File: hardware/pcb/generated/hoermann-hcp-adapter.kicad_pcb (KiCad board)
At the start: 2 copper layers, 65 x 44.5 mm, 6 parts, among them J1 HCP2 6P6C, U1 ESP32-C3 Super Mini, U2 Isolated RS485

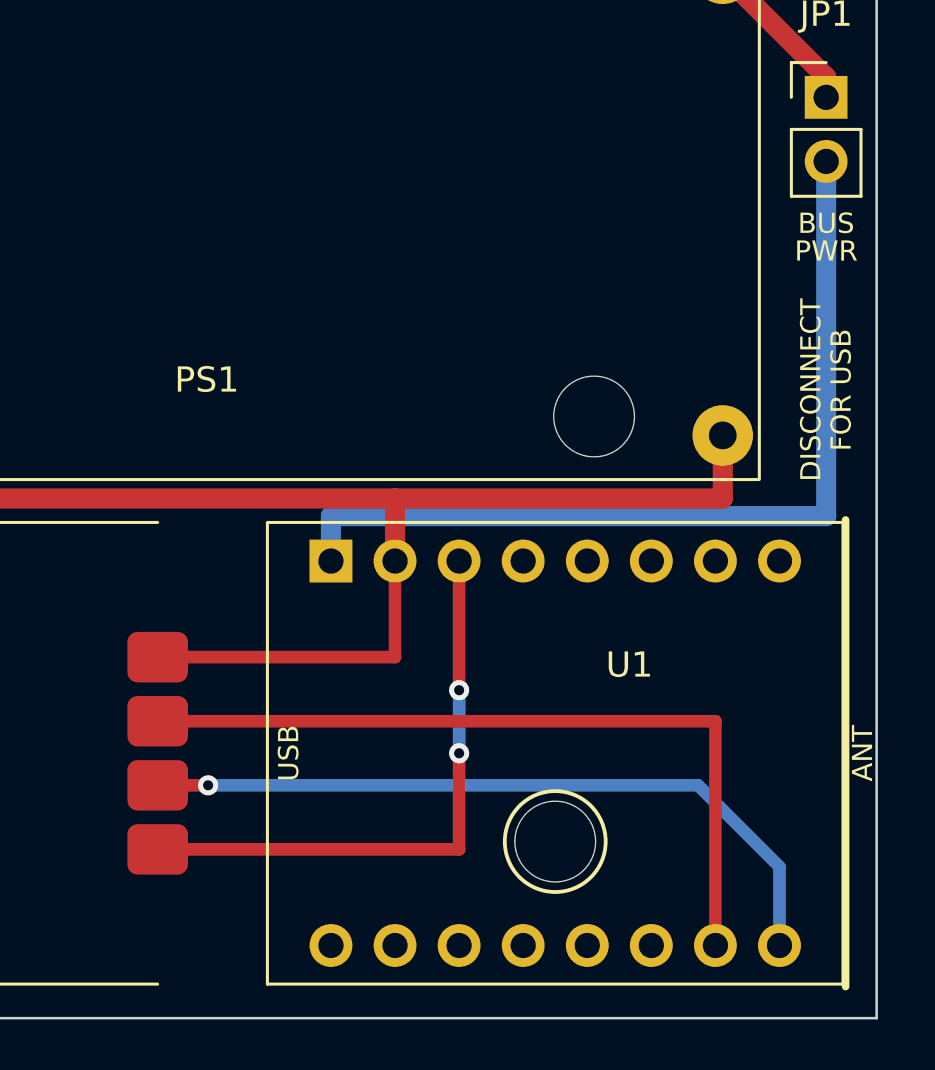
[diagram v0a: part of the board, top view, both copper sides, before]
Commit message: Put the ESP32 USB port at the board edge
U1 is rotated so its USB end sits flush with the right edge and stays
usable when mounted. The antenna now points towards the RS485 module.

Co-Authored-By: Claude Fable 5.1 <noreply@anthropic.com>
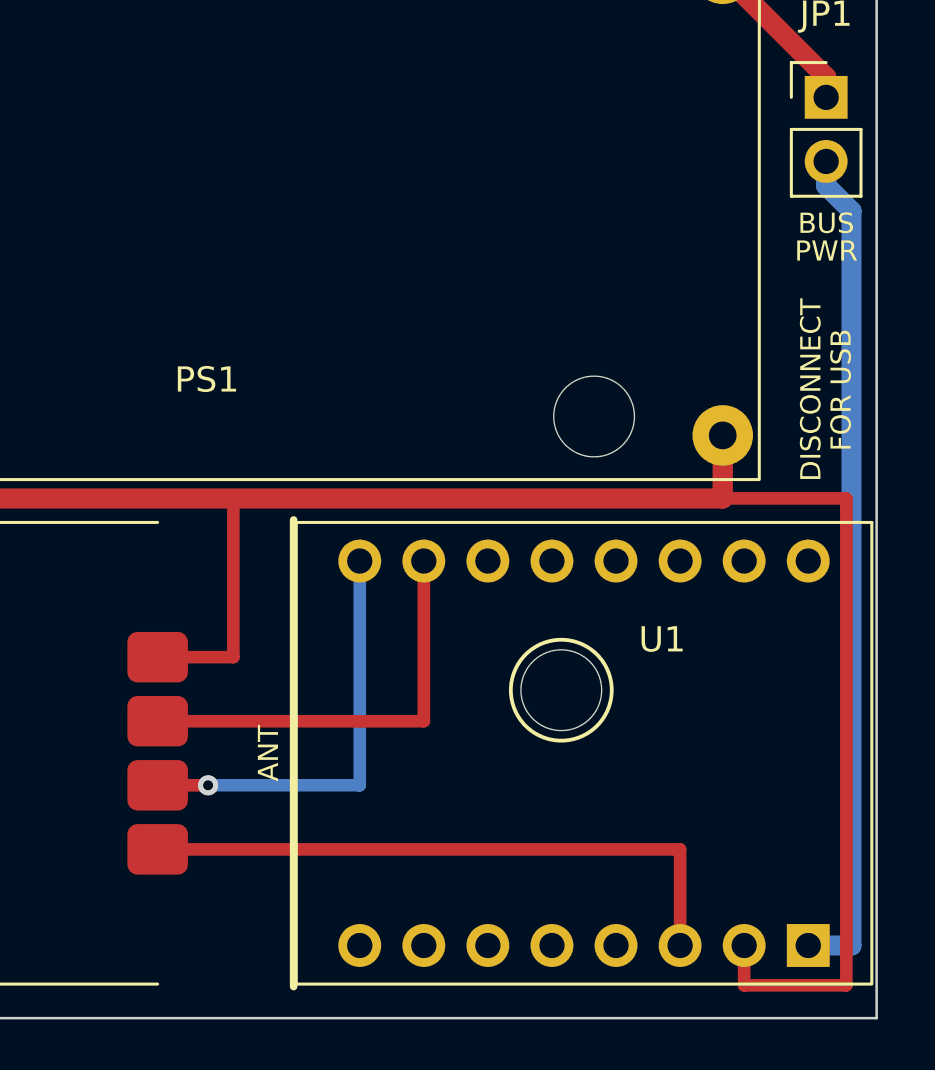
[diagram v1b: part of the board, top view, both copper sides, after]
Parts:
- moved H1 6.00 mm to (52.5, 31.5)
- moved U1 1.14 mm to (53.4, 34.0), turned to 270 degrees
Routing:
- net HCP_GND: track 76.0 -> 99.4 mm
- net UART_RX_GPIO20: track 31.0 -> 16.9 mm
- net UART_TX_GPIO21: track 29.1 -> 16.9 mm
- net ESP_5V: track 35.5 -> 33.2 mm
- net ESP_3V3: track 23.4 -> 24.5 mm, vias 2 -> 0
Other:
- board text removed: "USB"

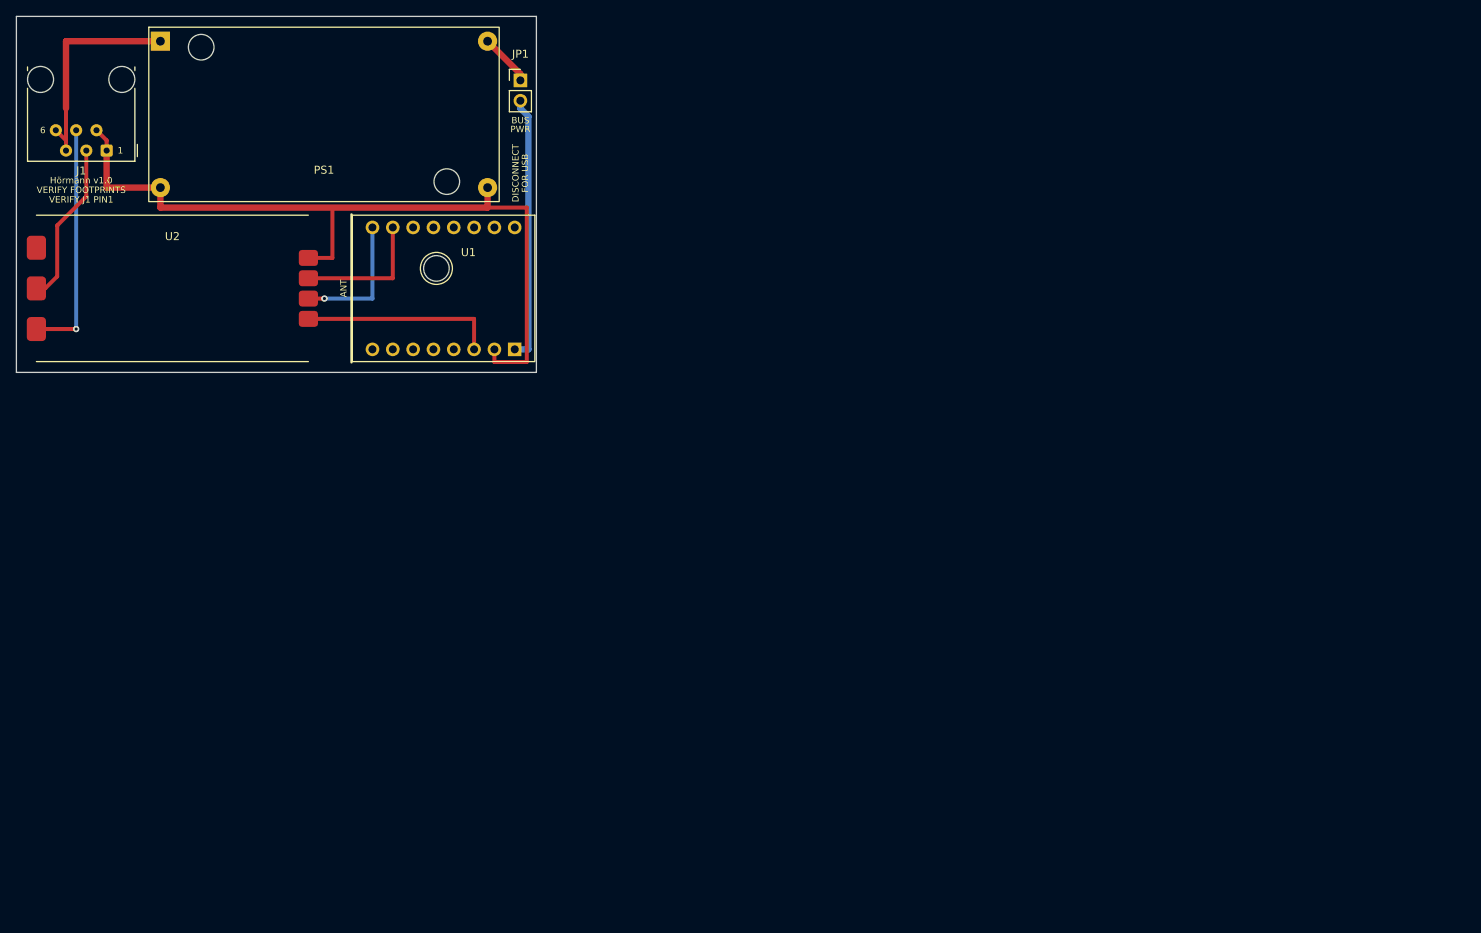
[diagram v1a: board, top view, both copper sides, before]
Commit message: Generate the schematic directly as KiCad file, centre the PCB plot
schematic.py replaces the SKiDL flow: symbols with named pins, routed
wires, net labels and ground symbols are written straight to .kicad_sch,
then kicad-cli runs ERC, exports the netlist (checked against design.py)
and renders the PDF. SKiDL and the vendored symbol library are gone.
The PCB now sits centred on the A4 sheet of the layer PDF.

Co-Authored-By: Claude Fable 5.1 <noreply@anthropic.com>
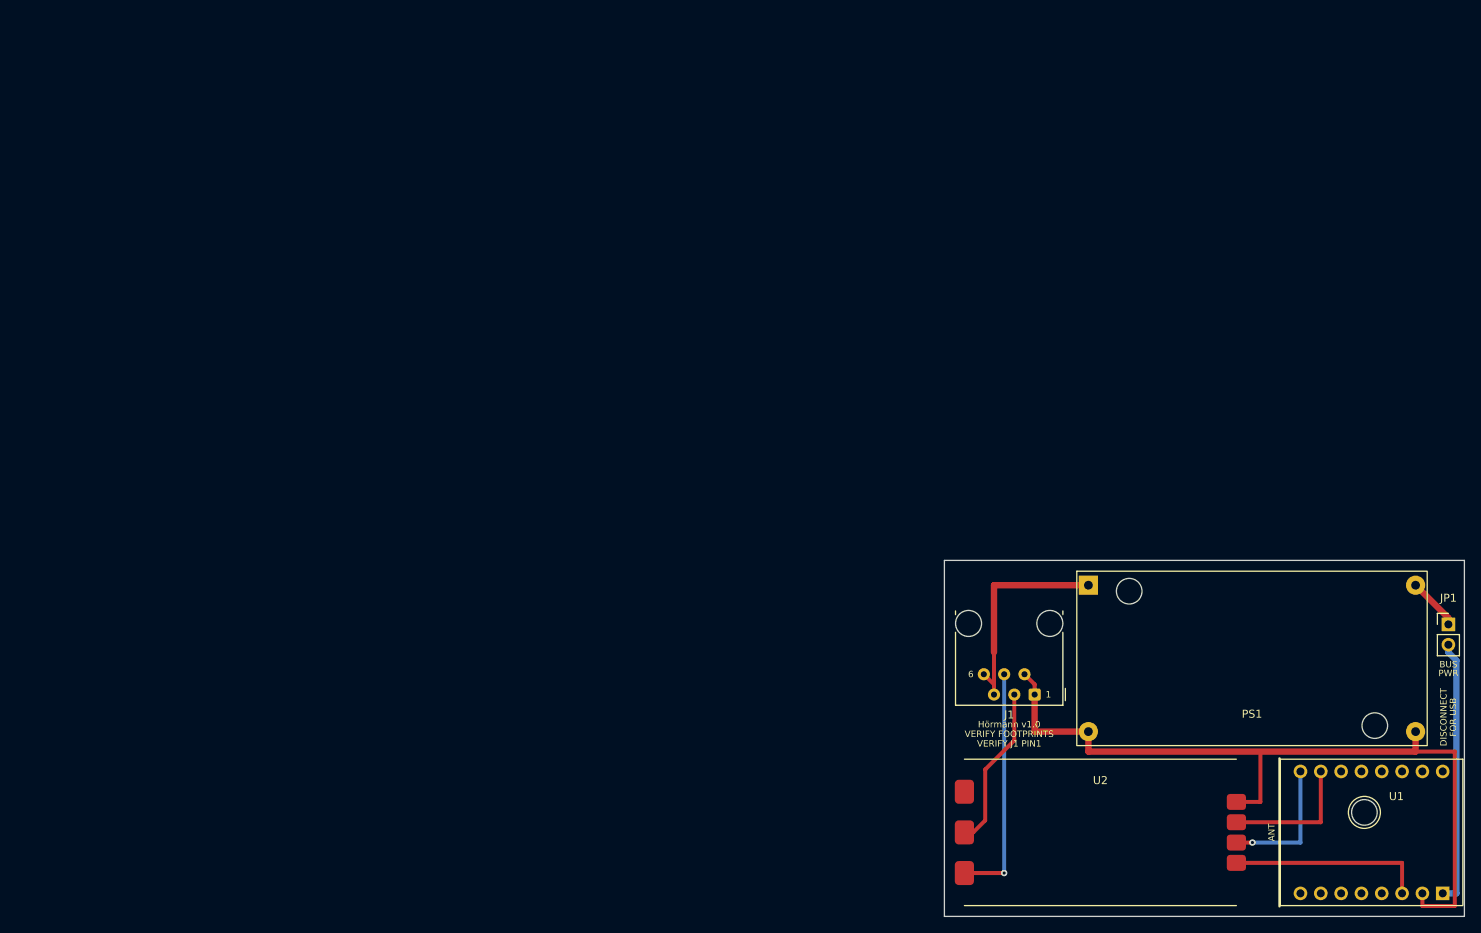
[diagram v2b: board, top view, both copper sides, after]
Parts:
- moved PS1 134.5 mm to (154.4, 80.2)
- moved H1 134.5 mm to (168.5, 99.5)
- moved J1 134.5 mm to (127.3, 84.8)
- moved JP1 134.5 mm to (179.0, 76.0)
- moved U1 134.5 mm to (169.4, 102.0)
- moved U2 134.5 mm to (135.5, 102.0)

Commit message: Regenerate outputs
Co-Authored-By: Claude Fable 5.1 <noreply@anthropic.com>
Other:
- board text added: "Hörmann HCP2 Adapter daa3d0a-dirty"
- board text added: "Hörmann daa3d0a-dirty"
- board text removed: "Hörmann HCP2 Adapter v1.0"
- board text removed: "Hörmann v1.0"
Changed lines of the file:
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@@
   (via (at 123.47 107.08) (size 0.8) (drill 0.4) (layers "F.Cu" "B.Cu") (net 3))
   (gr_rect (start 116.0 68.0) (end 181.0 112.5) (stroke (width 0.1) (type default)) (fill none) (layer "Edge.Cuts"))
-  (gr_text "Hörmann v1.0" (at 124.1 88.5 0) (layer "F.SilkS") (effects (font (size 0.8 0.8) (thickness 0.15))))
+  (gr_text "Hörmann daa3d0a-dirty" (at 124.1 88.5 0) (layer "F.SilkS") (effects (font (size 0.8 0.8) (thickness 0.15))))
   (gr_text "VERIFY FOOTPRINTS" (at 124.1 89.7 0) (layer "F.SilkS") (effects (font (size 0.8 0.8) (thickness 0.15))))
   (gr_text "VERIFY J1 PIN1" (at 124.1 90.9 0) (layer "F.SilkS") (effects (font (size 0.8 0.8) (thickness 0.15))))
@@
   (gr_text "FOR USB" (at 179.6 87.6 90) (layer "F.SilkS") (effects (font (size 0.8 0.8) (thickness 0.15))))
   (gr_text "ANT" (at 156.9 102.0 90) (layer "F.SilkS") (effects (font (size 0.8 0.8) (thickness 0.15))))
-  (gr_text "Hörmann HCP2 Adapter v1.0" (at 141.0 98.5 0) (layer "B.SilkS") (effects (font (size 1.5 1.5) (thickness 0.15)) (justify mirror)))
+  (gr_text "Hörmann HCP2 Adapter daa3d0a-dirty" (at 141.0 98.5 0) (layer "B.SilkS") (effects (font (size 1.5 1.5) (thickness 0.15)) (justify mirror)))
   (gr_text "(C) 2026 Thies Gerken" (at 141.0 101.5 0) (layer "B.SilkS") (effects (font (size 1.2 1.2) (thickness 0.15)) (justify mirror)))
   (embedded_fonts no)

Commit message: Regenerate outputs
Co-Authored-By: Claude Fable 5.1 <noreply@anthropic.com>
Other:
- board text added: "Hörmann 7fe4161"
- board text added: "Hörmann HCP2 Adapter 7fe4161"
- board text removed: "Hörmann HCP2 Adapter daa3d0a-dirty"
- board text removed: "Hörmann daa3d0a-dirty"
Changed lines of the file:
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@@
   (via (at 123.47 107.08) (size 0.8) (drill 0.4) (layers "F.Cu" "B.Cu") (net 3))
   (gr_rect (start 116.0 68.0) (end 181.0 112.5) (stroke (width 0.1) (type default)) (fill none) (layer "Edge.Cuts"))
-  (gr_text "Hörmann daa3d0a-dirty" (at 124.1 88.5 0) (layer "F.SilkS") (effects (font (size 0.8 0.8) (thickness 0.15))))
+  (gr_text "Hörmann 7fe4161" (at 124.1 88.5 0) (layer "F.SilkS") (effects (font (size 0.8 0.8) (thickness 0.15))))
   (gr_text "VERIFY FOOTPRINTS" (at 124.1 89.7 0) (layer "F.SilkS") (effects (font (size 0.8 0.8) (thickness 0.15))))
   (gr_text "VERIFY J1 PIN1" (at 124.1 90.9 0) (layer "F.SilkS") (effects (font (size 0.8 0.8) (thickness 0.15))))
@@
   (gr_text "FOR USB" (at 179.6 87.6 90) (layer "F.SilkS") (effects (font (size 0.8 0.8) (thickness 0.15))))
   (gr_text "ANT" (at 156.9 102.0 90) (layer "F.SilkS") (effects (font (size 0.8 0.8) (thickness 0.15))))
-  (gr_text "Hörmann HCP2 Adapter daa3d0a-dirty" (at 141.0 98.5 0) (layer "B.SilkS") (effects (font (size 1.5 1.5) (thickness 0.15)) (justify mirror)))
+  (gr_text "Hörmann HCP2 Adapter 7fe4161" (at 141.0 98.5 0) (layer "B.SilkS") (effects (font (size 1.5 1.5) (thickness 0.15)) (justify mirror)))
   (gr_text "(C) 2026 Thies Gerken" (at 141.0 101.5 0) (layer "B.SilkS") (effects (font (size 1.2 1.2) (thickness 0.15)) (justify mirror)))
   (embedded_fonts no)

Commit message: Regenerate outputs
Co-Authored-By: Claude Fable 5.1 <noreply@anthropic.com>
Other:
- board text added: "Hörmann 0d17945"
- board text added: "Hörmann HCP2 Adapter 0d17945"
- board text removed: "Hörmann 7fe4161"
- board text removed: "Hörmann HCP2 Adapter 7fe4161"
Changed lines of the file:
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@@
   (via (at 123.47 107.08) (size 0.8) (drill 0.4) (layers "F.Cu" "B.Cu") (net 3))
   (gr_rect (start 116.0 68.0) (end 181.0 112.5) (stroke (width 0.1) (type default)) (fill none) (layer "Edge.Cuts"))
-  (gr_text "Hörmann 7fe4161" (at 124.1 88.5 0) (layer "F.SilkS") (effects (font (size 0.8 0.8) (thickness 0.15))))
+  (gr_text "Hörmann 0d17945" (at 124.1 88.5 0) (layer "F.SilkS") (effects (font (size 0.8 0.8) (thickness 0.15))))
   (gr_text "VERIFY FOOTPRINTS" (at 124.1 89.7 0) (layer "F.SilkS") (effects (font (size 0.8 0.8) (thickness 0.15))))
   (gr_text "VERIFY J1 PIN1" (at 124.1 90.9 0) (layer "F.SilkS") (effects (font (size 0.8 0.8) (thickness 0.15))))
@@
   (gr_text "FOR USB" (at 179.6 87.6 90) (layer "F.SilkS") (effects (font (size 0.8 0.8) (thickness 0.15))))
   (gr_text "ANT" (at 156.9 102.0 90) (layer "F.SilkS") (effects (font (size 0.8 0.8) (thickness 0.15))))
-  (gr_text "Hörmann HCP2 Adapter 7fe4161" (at 141.0 98.5 0) (layer "B.SilkS") (effects (font (size 1.5 1.5) (thickness 0.15)) (justify mirror)))
+  (gr_text "Hörmann HCP2 Adapter 0d17945" (at 141.0 98.5 0) (layer "B.SilkS") (effects (font (size 1.5 1.5) (thickness 0.15)) (justify mirror)))
   (gr_text "(C) 2026 Thies Gerken" (at 141.0 101.5 0) (layer "B.SilkS") (effects (font (size 1.2 1.2) (thickness 0.15)) (justify mirror)))
   (embedded_fonts no)

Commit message: Regenerate outputs
Co-Authored-By: Claude Fable 5.1 <noreply@anthropic.com>
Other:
- board text added: "Hörmann 1b34439"
- board text added: "Hörmann HCP2 Adapter 1b34439"
- board text removed: "Hörmann 0d17945"
- board text removed: "Hörmann HCP2 Adapter 0d17945"
- board text removed: "VERIFY J1 PIN1"
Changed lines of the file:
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@@
   (via (at 123.47 107.08) (size 0.8) (drill 0.4) (layers "F.Cu" "B.Cu") (net 3))
   (gr_rect (start 116.0 68.0) (end 181.0 112.5) (stroke (width 0.1) (type default)) (fill none) (layer "Edge.Cuts"))
-  (gr_text "Hörmann 0d17945" (at 124.1 88.5 0) (layer "F.SilkS") (effects (font (size 0.8 0.8) (thickness 0.15))))
+  (gr_text "Hörmann 1b34439" (at 124.1 88.5 0) (layer "F.SilkS") (effects (font (size 0.8 0.8) (thickness 0.15))))
   (gr_text "VERIFY FOOTPRINTS" (at 124.1 89.7 0) (layer "F.SilkS") (effects (font (size 0.8 0.8) (thickness 0.15))))
-  (gr_text "VERIFY J1 PIN1" (at 124.1 90.9 0) (layer "F.SilkS") (effects (font (size 0.8 0.8) (thickness 0.15))))
   (gr_text "1" (at 129.0 84.77 0) (layer "F.SilkS") (effects (font (size 0.8 0.8) (thickness 0.15))))
   (gr_text "6" (at 119.3 82.23 0) (layer "F.SilkS") (effects (font (size 0.8 0.8) (thickness 0.15))))
@@
   (gr_text "FOR USB" (at 179.6 87.6 90) (layer "F.SilkS") (effects (font (size 0.8 0.8) (thickness 0.15))))
   (gr_text "ANT" (at 156.9 102.0 90) (layer "F.SilkS") (effects (font (size 0.8 0.8) (thickness 0.15))))
-  (gr_text "Hörmann HCP2 Adapter 0d17945" (at 141.0 98.5 0) (layer "B.SilkS") (effects (font (size 1.5 1.5) (thickness 0.15)) (justify mirror)))
+  (gr_text "Hörmann HCP2 Adapter 1b34439" (at 141.0 98.5 0) (layer "B.SilkS") (effects (font (size 1.5 1.5) (thickness 0.15)) (justify mirror)))
   (gr_text "(C) 2026 Thies Gerken" (at 141.0 101.5 0) (layer "B.SilkS") (effects (font (size 1.2 1.2) (thickness 0.15)) (justify mirror)))
   (embedded_fonts no)

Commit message: Regenerate outputs
Co-Authored-By: Claude Fable 5.1 <noreply@anthropic.com>
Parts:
- J1: footprint HCP:RJ12_Amphenol_54601-x06_Horizontal -> HCP:RJ12_95001_6P6C
- moved J1 16.9 mm to (125.0, 68.0), turned to 0 degrees
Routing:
- net HCP_B_MINUS: track 20.5 -> 33.8 mm
- net HCP_25V: track 28.5 -> 15.6 mm
- net HCP_GND: track 99.4 -> 109.1 mm
- net HCP_A_PLUS: track 29.8 -> 35.2 mm, vias 1 -> 0
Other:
- board text added: "Hörmann 33cb4bf"
- board text added: "Hörmann HCP2 Adapter 33cb4bf"
- board text removed: "6"
- board text removed: "Hörmann 1b34439"
- board text removed: "Hörmann HCP2 Adapter 1b34439"

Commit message: Regenerate outputs
Co-Authored-By: Claude Fable 5.1 <noreply@anthropic.com>
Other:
- board text added: "Hörmann 93a904b"
- board text added: "Hörmann HCP2 Adapter 93a904b"
- board text removed: "Hörmann 33cb4bf"
- board text removed: "Hörmann HCP2 Adapter 33cb4bf"
- board text removed: "VERIFY FOOTPRINTS"
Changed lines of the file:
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@@
     (fp_rect (start -6.35 -0.25) (end 6.35 13.25) (stroke (width 0.05) (type default)) (fill none) (layer "F.CrtYd"))
     (fp_text user "PCB EDGE" (at 0 1.2 0) (layer "F.Fab") (effects (font (size 0.6 0.6) (thickness 0.10))))
-    (fp_text user "VERIFY 6P6C DIMS" (at 0 3.5 0) (layer "F.Fab") (effects (font (size 0.6 0.6) (thickness 0.10))))
     (fp_text user "${REFERENCE}" (at 0 7.0 0) (layer "F.Fab") (effects (font (size 0.8 0.8) (thickness 0.12))))
     (embedded_fonts no)
@@
     (pad "" np_thru_hole circle (at -15.35 -8.4) (size 3.2 3.2) (drill 3.2) (layers "*.Cu" "*.Mask"))
     (pad "" np_thru_hole circle (at 15.35 8.4) (size 3.2 3.2) (drill 3.2) (layers "*.Cu" "*.Mask"))
-    (fp_text user "VERIFY PAD/HOLE POS" (at 0 4.5 0) (layer "F.Fab") (effects (font (size 0.8 0.8) (thickness 0.12))))
     (fp_text user "${REFERENCE}" (at 0 0 0) (layer "F.Fab") (effects (font (size 0.8 0.8) (thickness 0.12))))
     (embedded_fonts no)
@@
     (pad "7" smd roundrect (at 17 5.08 180) (size 2.4 3.0) (layers "F.Cu" "F.Paste" "F.Mask") (roundrect_rratio 0.2))
     (fp_text user "EARTH/NC" (at 13.2 5.08 0) (layer "F.Fab") (effects (font (size 0.6 0.6) (thickness 0.10))))
-    (fp_text user "VERIFY PAD POS" (at 0 6.5 0) (layer "F.Fab") (effects (font (size 0.8 0.8) (thickness 0.12))))
     (fp_text user "${REFERENCE}" (at 0 0 0) (layer "F.Fab") (effects (font (size 0.8 0.8) (thickness 0.12))))
     (embedded_fonts no)
@@
   (via (at 154.5 103.27) (size 0.8) (drill 0.4) (layers "F.Cu" "B.Cu") (net 8))
   (gr_rect (start 116.0 68.0) (end 181.0 112.5) (stroke (width 0.1) (type default)) (fill none) (layer "Edge.Cuts"))
-  (gr_text "Hörmann 33cb4bf" (at 125.0 84.0 0) (layer "F.SilkS") (effects (font (size 0.8 0.8) (thickness 0.15))))
-  (gr_text "VERIFY FOOTPRINTS" (at 125.0 85.2 0) (layer "F.SilkS") (effects (font (size 0.8 0.8) (thickness 0.15))))
+  (gr_text "Hörmann 93a904b" (at 125.0 84.0 0) (layer "F.SilkS") (effects (font (size 0.8 0.8) (thickness 0.15))))
   (gr_text "1" (at 122.45 80.6 0) (layer "F.SilkS") (effects (font (size 0.8 0.8) (thickness 0.15))))
   (gr_text "BUS" (at 179.0 81.0 0) (layer "F.SilkS") (effects (font (size 0.8 0.8) (thickness 0.15))))
@@
   (gr_text "FOR USB" (at 179.6 87.6 90) (layer "F.SilkS") (effects (font (size 0.8 0.8) (thickness 0.15))))
   (gr_text "ANT" (at 156.9 102.0 90) (layer "F.SilkS") (effects (font (size 0.8 0.8) (thickness 0.15))))
-  (gr_text "Hörmann HCP2 Adapter 33cb4bf" (at 141.0 98.5 0) (layer "B.SilkS") (effects (font (size 1.5 1.5) (thickness 0.15)) (justify mirror)))
+  (gr_text "Hörmann HCP2 Adapter 93a904b" (at 141.0 98.5 0) (layer "B.SilkS") (effects (font (size 1.5 1.5) (thickness 0.15)) (justify mirror)))
   (gr_text "(C) 2026 Thies Gerken" (at 141.0 101.5 0) (layer "B.SilkS") (effects (font (size 1.2 1.2) (thickness 0.15)) (justify mirror)))
   (embedded_fonts no)
